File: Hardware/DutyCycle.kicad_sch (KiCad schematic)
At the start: 46 parts, among them J1 LiPo, J2 USB, J4 MOT, Q1 AO3400A, Q2 AO3400A, Q3 AO3401A, SW1 SW_Push, U1 AT32F421KxU7, U2 CH340E, U3 ME6211C28M5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

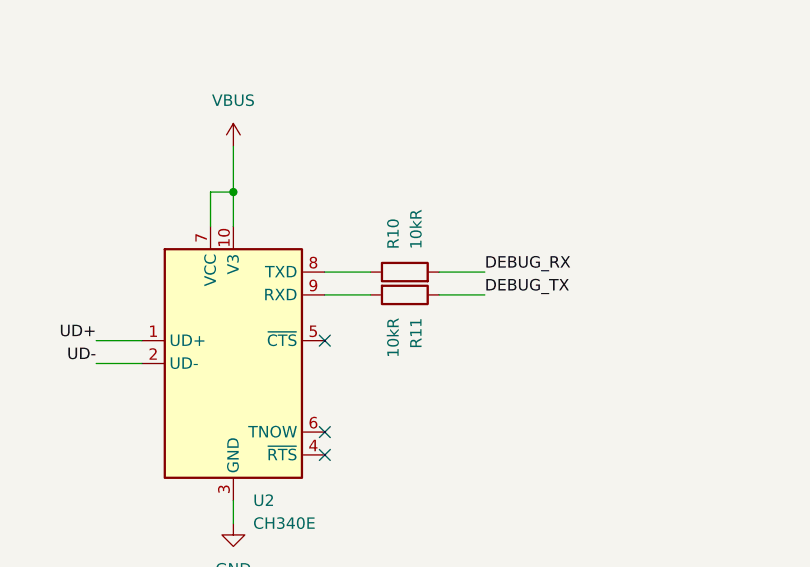
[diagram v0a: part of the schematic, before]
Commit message: fix(Hardware): fix CH340E RES 10kR -> 100R
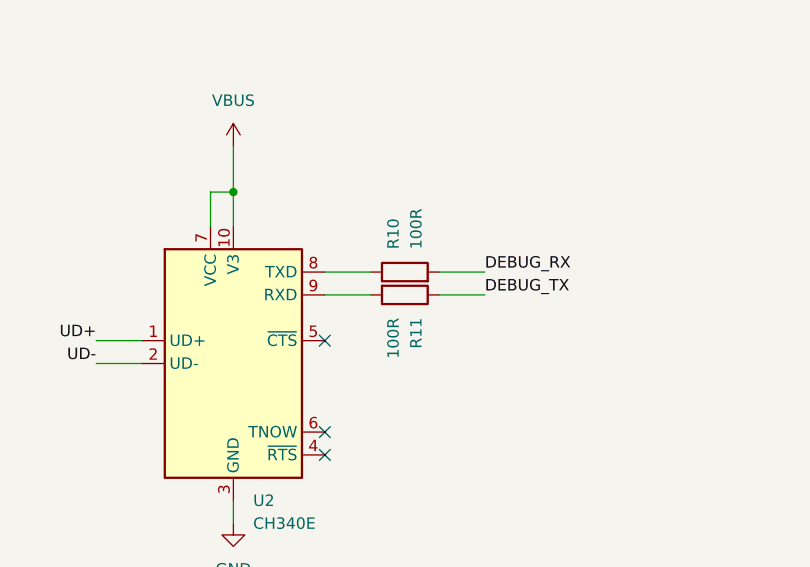
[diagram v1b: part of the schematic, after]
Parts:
- R10, R11: value 10kR -> 100R
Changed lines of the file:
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@@
 			)
 		)
-		(property "Value" "10kR"
+		(property "Value" "100R"
 			(at 254.0001 232.41 0)
 			(effects
@@
 			)
 		)
-		(property "Value" "10kR"
+		(property "Value" "100R"
 			(at 256.5399 224.79 0)
 			(effects

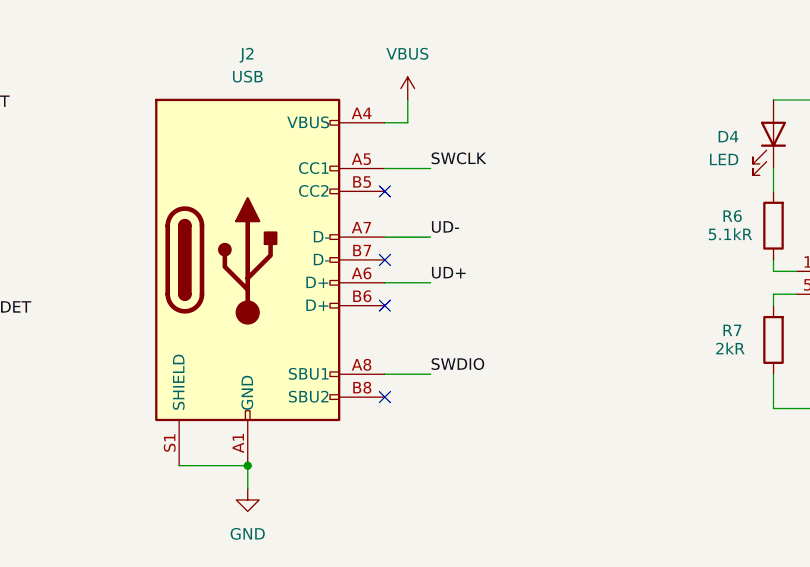
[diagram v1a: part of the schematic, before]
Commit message: feat(Hardware): add support for USB insertion in both directions
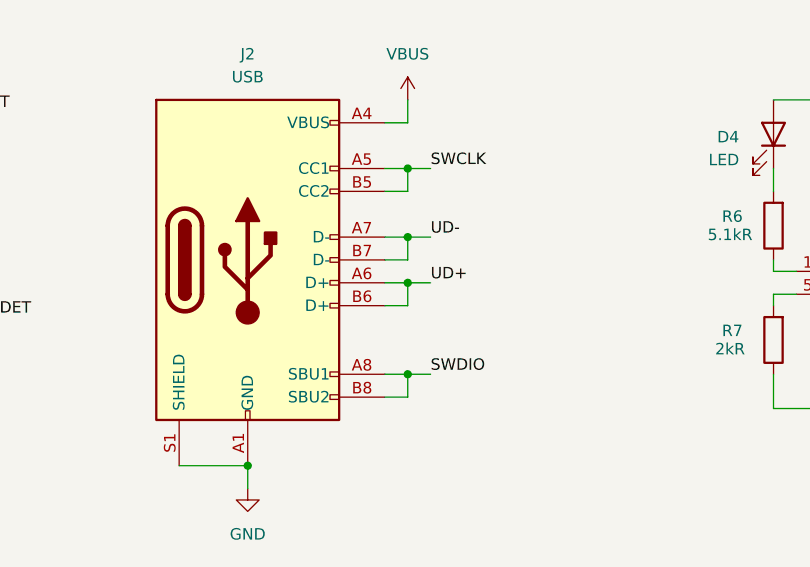
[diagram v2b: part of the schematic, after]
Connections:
- net SWCLK: now also J2.B5 (CC2)
- net SWDIO: now also J2.B8 (SBU2)
- net UD+: now also J2.B6 (D+)
- net UD-: now also J2.B7 (D-)
- no-connect marks 22 -> 18
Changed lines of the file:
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@@
+	)
+	(junction
+		(at 180.34 69.85)
+		(diameter 0)
+		(color 0 0 0 0)
 	)
 	(junction
@@
 	)
 	(junction
+		(at 180.34 54.61)
+		(diameter 0)
+		(color 0 0 0 0)
+	)
+	(junction
 		(at 168.91 161.29)
 		(diameter 0)
@@
 	)
 	(junction
+		(at 180.34 59.69)
+		(diameter 0)
+		(color 0 0 0 0)
+	)
+	(junction
 		(at 233.68 39.37)
 		(diameter 0)
@@
 	)
 	(junction
+		(at 180.34 46.99)
+		(diameter 0)
+		(color 0 0 0 0)
+	)
+	(junction
 		(at 236.22 130.81)
 		(diameter 0)
@@
 	)
 	(no_connect
-		(at 177.8 72.39)
-	)
-	(no_connect
 		(at 246.38 245.11)
 	)
@@
 	)
 	(no_connect
-		(at 177.8 62.23)
-	)
-	(no_connect
 		(at 223.52 163.83)
 	)
@@
 	)
 	(no_connect
-		(at 177.8 57.15)
-	)
-	(no_connect
 		(at 248.92 161.29)
 	)
 	(no_connect
-		(at 177.8 49.53)
-	)
-	(no_connect
 		(at 223.52 179.07)
 	)
@@
 	(wire
 		(pts
-			(xy 177.8 54.61) (xy 182.88 54.61)
+			(xy 177.8 62.23) (xy 180.34 62.23)
+		)
+		(stroke
+			(width 0)
+			(type default)
+		)
+	)
+	(wire
+		(pts
+			(xy 177.8 54.61) (xy 180.34 54.61)
 		)
 		(stroke
@@
 	(wire
 		(pts
+			(xy 180.34 46.99) (xy 182.88 46.99)
+		)
+		(stroke
+			(width 0)
+			(type default)
+		)
+	)
+	(wire
+		(pts
+			(xy 180.34 69.85) (xy 182.88 69.85)
+		)
+		(stroke
+			(width 0)
+			(type default)
+		)
+	)
+	(wire
+		(pts
 			(xy 233.68 73.66) (xy 233.68 68.58)
 		)
@@
 	(wire
 		(pts
-			(xy 177.8 46.99) (xy 182.88 46.99)
+			(xy 177.8 46.99) (xy 180.34 46.99)
 		)
 		(stroke
@@
 	(wire
 		(pts
+			(xy 177.8 57.15) (xy 180.34 57.15)
+		)
+		(stroke
+			(width 0)
+			(type default)
+		)
+	)
+	(wire
+		(pts
 			(xy 246.38 227.33) (xy 251.46 227.33)
 		)
@@
 	(wire
 		(pts
+			(xy 180.34 72.39) (xy 180.34 69.85)
+		)
+		(stroke
+			(width 0)
+			(type default)
+		)
+	)
+	(wire
+		(pts
 			(xy 74.93 86.36) (xy 74.93 90.17)
 		)
@@
 	(wire
 		(pts
+			(xy 180.34 49.53) (xy 180.34 46.99)
+		)
+		(stroke
+			(width 0)
+			(type default)
+		)
+	)
+	(wire
+		(pts
 			(xy 326.39 63.5) (xy 326.39 67.31)
 		)
@@
 	(wire
 		(pts
+			(xy 177.8 72.39) (xy 180.34 72.39)
+		)
+		(stroke
+			(width 0)
+			(type default)
+		)
+	)
+	(wire
+		(pts
 			(xy 176.53 161.29) (xy 168.91 161.29)
 		)
@@
 	(wire
 		(pts
+			(xy 180.34 57.15) (xy 180.34 54.61)
+		)
+		(stroke
+			(width 0)
+			(type default)
+		)
+	)
+	(wire
+		(pts
 			(xy 101.6 63.5) (xy 106.68 63.5)
 		)
@@
 	(wire
 		(pts
-			(xy 177.8 59.69) (xy 182.88 59.69)
+			(xy 177.8 59.69) (xy 180.34 59.69)
 		)
 		(stroke
@@
 	(wire
 		(pts
-			(xy 177.8 69.85) (xy 182.88 69.85)
+			(xy 177.8 69.85) (xy 180.34 69.85)
 		)
 		(stroke
@@
 	(wire
 		(pts
+			(xy 180.34 59.69) (xy 182.88 59.69)
+		)
+		(stroke
+			(width 0)
+			(type default)
+		)
+	)
+	(wire
+		(pts
 			(xy 236.22 252.73) (xy 236.22 255.27)
 		)
@@
 	(wire
 		(pts
+			(xy 177.8 49.53) (xy 180.34 49.53)
+		)
+		(stroke
+			(width 0)
+			(type default)
+		)
+	)
+	(wire
+		(pts
 			(xy 304.8 67.31) (xy 326.39 67.31)
 		)
@@
 	(wire
 		(pts
+			(xy 180.34 54.61) (xy 182.88 54.61)
+		)
+		(stroke
+			(width 0)
+			(type default)
+		)
+	)
+	(wire
+		(pts
 			(xy 295.91 53.34) (xy 304.8 53.34)
 		)
@@
 		)
 		(stroke
+			(width 0)
+			(type default)
+		)
+	)
+	(wire
+		(pts
+			(xy 180.34 62.23) (xy 180.34 59.69)
+		)
+		(stroke
